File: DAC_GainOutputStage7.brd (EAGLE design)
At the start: 110 x 110.3 mm, 78 parts, among them J1 1935190, J3 SJ-63033A, U1 LM317MQDCYR, U2 LM317MQDCYR

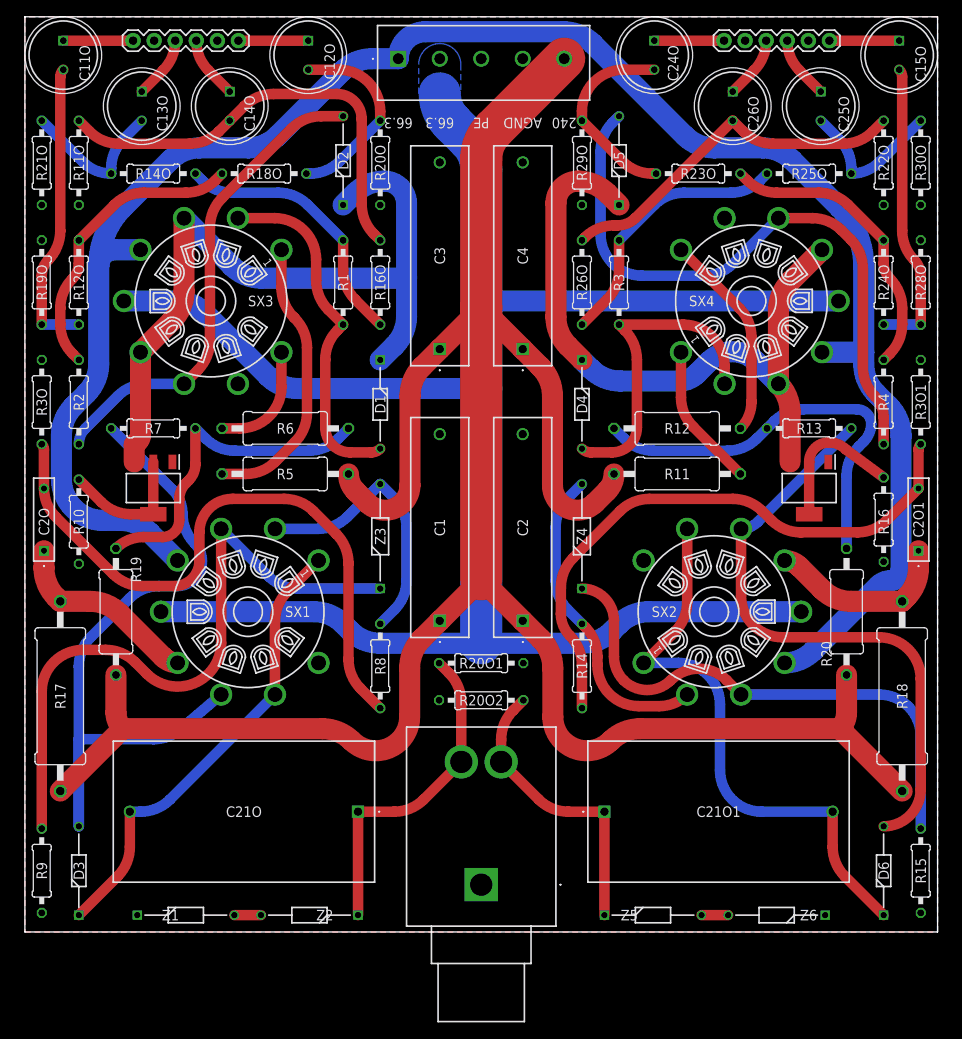
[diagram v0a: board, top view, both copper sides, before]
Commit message: Added new spice model and work on output stage
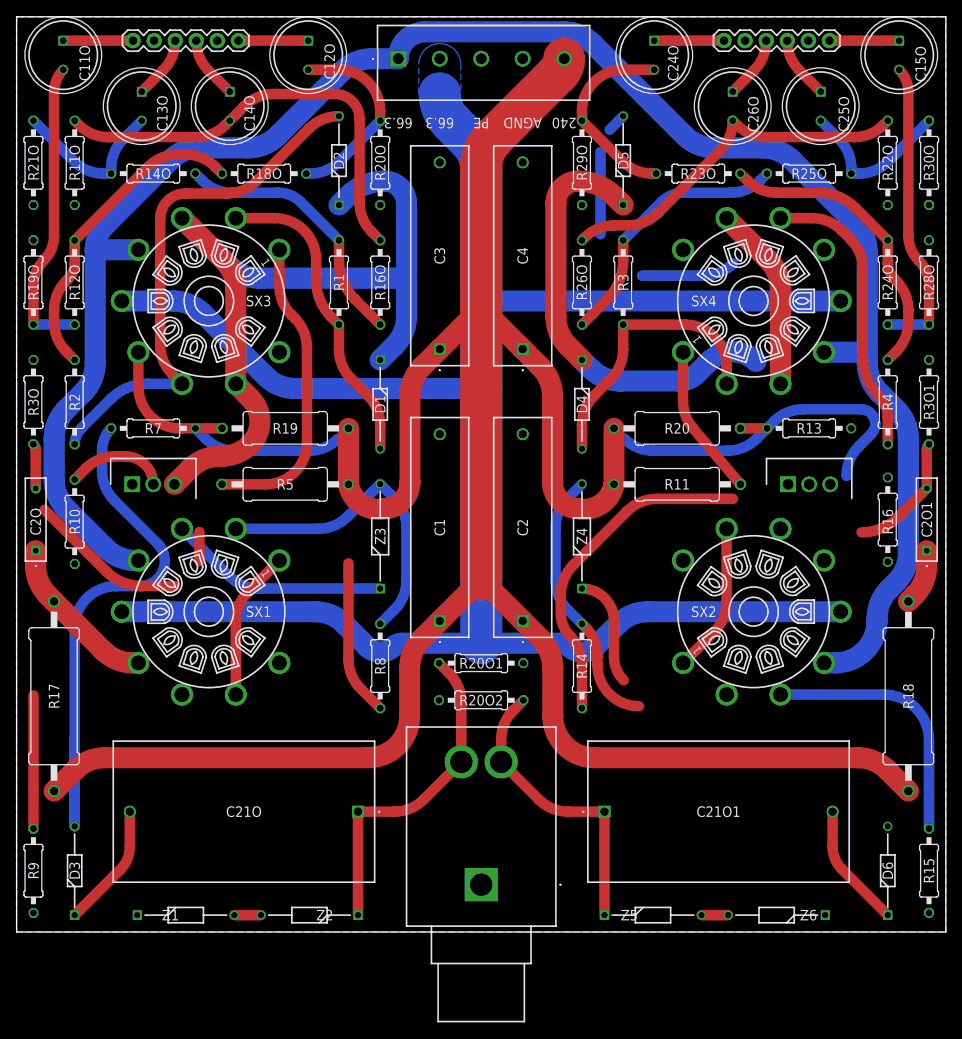
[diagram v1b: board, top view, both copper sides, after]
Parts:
- removed R12, R6: 3k, Dual Mono Amp Library:0411/15
- R11, R5: value 18k -> 15k
- U1, U2: value LM317MQDCYR -> LM317MTG; device Dual Mono Amp Library:SOT230P700X180-4N -> Dual Mono Amp Library:TO254P482X997X2018-3P
- moved R19 30.1 mm to (31.4, 55.7), turned to 0 degrees
- moved R20 30.1 mm to (78.6, 55.7), turned to 0 degrees
- moved SX2 4.76 mm to (87.8, 33.6)
- moved SX1 4.72 mm to (22.2, 33.6)
- moved U2 2.58 mm to (92.0, 49.0), turned to 0 degrees
- moved U1 2.58 mm to (12.9, 49.0), turned to 0 degrees
- moved R11 1.25 mm to (78.6, 49.0)
- moved R5 1.25 mm to (31.4, 49.0)
- moved R19O 1.00 mm to (1.03, 73.3)
- moved R21O 1.00 mm to (1.03, 87.7)
- moved R3O 1.00 mm to (1.03, 58.9)
- moved R9 1.00 mm to (1.03, 2.38)
- moved C2O1 1.00 mm to (108.7, 40.9)
- moved R15 1.00 mm to (109.0, 2.38)
- moved R28O 1.00 mm to (109.0, 73.3)
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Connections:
- removed net N$43: R6.1, SX3.9
- removed net N$44: R12.1, SX4.9
- net N$1: now also SX3.6; no longer R6.2
- net N$22: now also SX3.8; no longer SX3.6
- net N$37: no longer U1.4
- net N$38: no longer U2.4
- net N$7: now also SX4.8; no longer SX4.6
- net N$9: now also SX4.6; no longer R12.2
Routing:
- net N$29: track 71.6 -> 0.00 mm
- net N$26: track 77.5 -> 42.6 mm
- net N$3: track 67.6 -> 33.0 mm
- net N$16: track 76.4 -> 46.7 mm
- net N$44: track 25.0 -> 0.00 mm
- net N$18: track 55.7 -> 33.0 mm
- net N$23: track 88.1 -> 66.5 mm
- net N$27: track 62.6 -> 43.7 mm
- net N$5: track 75.8 -> 58.3 mm
- net N$38: track 17.5 -> 0.00 mm
- net N$17: track 71.5 -> 55.3 mm
- net N$40: track 22.3 -> 6.71 mm
- net N$43: track 13.4 -> 0.00 mm
- net 66.3VAC/2: track 236.7 -> 247.8 mm
- net N$22: track 90.5 -> 100.6 mm
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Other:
- board size 110 x 110.3 mm -> 112 x 110.3 mm

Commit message: Finished new output stage?
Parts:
- moved R16 0.25 mm to (104.0, 44.4)
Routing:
- net N$29: track 0.00 -> 66.2 mm
- net N$3: track 33.0 -> 66.0 mm
- net N$26: track 42.6 -> 71.5 mm
- net N$18: track 33.0 -> 57.0 mm
- net N$27: track 43.7 -> 62.3 mm
- net N$1: track 34.6 -> 16.3 mm
- net N$16: track 46.7 -> 64.7 mm
- net N$5: track 58.3 -> 76.1 mm
- net N$7: track 74.7 -> 92.4 mm
- net N$9: track 43.2 -> 27.3 mm
- net N$17: track 55.3 -> 69.2 mm
- net N$14: track 31.3 -> 43.6 mm
- net N$38: track 0.00 -> 11.7 mm
- net N$40: track 6.71 -> 18.3 mm
- net N$23: track 66.5 -> 68.9 mm
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
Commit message: Finished boards and spice models
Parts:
- R15, R9: value 698 -> 249
- R17, R18: value 1k -> 402
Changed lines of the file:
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@@
 <attribute name="NAME" x="42.825" y="27.052625" locked="yes" size="1.27" layer="25" rot="R270" align="center"/>
 </element>
-<element name="R9" library="Dual Mono Amp Library" library_urn="urn:adsk.eagle:library:47621477" package="0207/10" package3d_urn="urn:adsk.eagle:package:23491/2" value="698" x="1.030775" y="2.380775" locked="yes" smashed="yes" rot="R90">
-<attribute name="DESCRIPTION" value="Metal Film Resistors - Through Hole 698ohm 1% 0.6W Metal Film Resistor" x="1.030775" y="2.380775" locked="yes" size="1.778" layer="27" rot="R90" display="off"/>
+<element name="R9" library="Dual Mono Amp Library" library_urn="urn:adsk.eagle:library:47621477" package="0207/10" package3d_urn="urn:adsk.eagle:package:23491/2" value="249" x="1.030775" y="2.380775" locked="yes" smashed="yes" rot="R90">
+<attribute name="DESCRIPTION" value="Metal Film Resistors - Through Hole 249ohm 1% 0.6W Metal Film Resistor" x="1.030775" y="2.380775" locked="yes" size="1.778" layer="27" rot="R90" display="off"/>
 <attribute name="HEIGHT" value="mm" x="1.030775" y="2.380775" locked="yes" size="1.778" layer="27" rot="R90" display="off"/>
-<attribute name="MANUFACTURER_NAME" value="YAGEO" x="1.030775" y="2.380775" locked="yes" size="1.778" layer="27" rot="R90" display="off"/>
-<attribute name="MANUFACTURER_PART_NUMBER" value="MF0207FTE52-698R" x="1.030775" y="2.380775" locked="yes" size="1.778" layer="27" rot="R90" display="off"/>
+<attribute name="MANUFACTURER_NAME" value="VISHAY" x="1.030775" y="2.380775" locked="yes" size="1.778" layer="27" rot="R90" display="off"/>
+<attribute name="MANUFACTURER_PART_NUMBER" value="MBB02070C2490FRP00" x="1.030775" y="2.380775" locked="yes" size="1.778" layer="27" rot="R90" display="off"/>
 <attribute name="MOUSER_PART_NUMBER" value="" x="1.030775" y="2.380775" locked="yes" size="1.778" layer="27" rot="R90" display="off"/>
 <attribute name="MOUSER_PRICE-STOCK" value="" x="1.030775" y="2.380775" locked="yes" size="1.778" layer="27" rot="R90" display="off"/>
@@
 <attribute name="NAME" x="67.139346875" y="27.052625" locked="yes" size="1.27" layer="25" rot="R270" align="center"/>
 </element>
-<element name="R15" library="Dual Mono Amp Library" library_urn="urn:adsk.eagle:library:47621477" package="0207/10" package3d_urn="urn:adsk.eagle:package:23491/2" value="698" x="108.969225" y="2.380775" locked="yes" smashed="yes" rot="R90">
-<attribute name="DESCRIPTION" value="Metal Film Resistors - Through Hole 698ohm 1% 0.6W Metal Film Resistor" x="108.969225" y="2.380775" locked="yes" size="1.778" layer="27" rot="R90" display="off"/>
+<element name="R15" library="Dual Mono Amp Library" library_urn="urn:adsk.eagle:library:47621477" package="0207/10" package3d_urn="urn:adsk.eagle:package:23491/2" value="249" x="108.969225" y="2.380775" locked="yes" smashed="yes" rot="R90">
+<attribute name="DESCRIPTION" value="Metal Film Resistors - Through Hole 249ohm 1% 0.6W Metal Film Resistor" x="108.969225" y="2.380775" locked="yes" size="1.778" layer="27" rot="R90" display="off"/>
 <attribute name="HEIGHT" value="mm" x="108.969225" y="2.380775" locked="yes" size="1.778" layer="27" rot="R90" display="off"/>
-<attribute name="MANUFACTURER_NAME" value="YAGEO" x="108.969225" y="2.380775" locked="yes" size="1.778" layer="27" rot="R90" display="off"/>
-<attribute name="MANUFACTURER_PART_NUMBER" value="MF0207FTE52-698R" x="108.969225" y="2.380775" locked="yes" size="1.778" layer="27" rot="R90" display="off"/>
+<attribute name="MANUFACTURER_NAME" value="VISHAY" x="108.969225" y="2.380775" locked="yes" size="1.778" layer="27" rot="R90" display="off"/>
+<attribute name="MANUFACTURER_PART_NUMBER" value="MBB02070C2490FRP00" x="108.969225" y="2.380775" locked="yes" size="1.778" layer="27" rot="R90" display="off"/>
 <attribute name="MOUSER_PART_NUMBER" value="" x="108.969225" y="2.380775" locked="yes" size="1.778" layer="27" rot="R90" display="off"/>
 <attribute name="MOUSER_PRICE-STOCK" value="" x="108.969225" y="2.380775" locked="yes" size="1.778" layer="27" rot="R90" display="off"/>
@@
 <attribute name="NAME" x="67.139346875" y="42.68946875" locked="yes" size="1.27" layer="25" rot="R90" align="center"/>
 </element>
-<element name="R17" library="Dual Mono Amp Library" library_urn="urn:adsk.eagle:library:47621477" package="0617/22" package3d_urn="urn:adsk.eagle:package:23577/1" value="1k" x="3.515684375" y="23.415121875" locked="yes" smashed="yes" rot="R90">
-<attribute name="DESCRIPTION" value="Metal Film Resistors - Through Hole 1K OHM 2W 1%" x="3.515684375" y="23.415121875" locked="yes" size="1.778" layer="27" rot="R90" display="off"/>
+<element name="R17" library="Dual Mono Amp Library" library_urn="urn:adsk.eagle:library:47621477" package="0617/22" package3d_urn="urn:adsk.eagle:package:23577/1" value="402" x="3.515684375" y="23.415121875" locked="yes" smashed="yes" rot="R90">
+<attribute name="DESCRIPTION" value="Metal Film Resistors - Through Hole 402 OHM 2W 1%" x="3.515684375" y="23.415121875" locked="yes" size="1.778" layer="27" rot="R90" display="off"/>
 <attribute name="HEIGHT" value="mm" x="3.515684375" y="23.415121875" locked="yes" size="1.778" layer="27" rot="R90" display="off"/>
-<attribute name="MANUFACTURER_NAME" value="YAGEO" x="3.515684375" y="23.415121875" locked="yes" size="1.778" layer="27" rot="R90" display="off"/>
-<attribute name="MANUFACTURER_PART_NUMBER" value="MFR200FRF52-1K" x="3.515684375" y="23.415121875" locked="yes" size="1.778" layer="27" rot="R90" display="off"/>
+<attribute name="MANUFACTURER_NAME" value="VISHAY" x="3.515684375" y="23.415121875" locked="yes" size="1.778" layer="27" rot="R90" display="off"/>
+<attribute name="MANUFACTURER_PART_NUMBER" value="RWR80S4020FRB12" x="3.515684375" y="23.415121875" locked="yes" size="1.778" layer="27" rot="R90" display="off"/>
 <attribute name="MOUSER_PART_NUMBER" value="" x="3.515684375" y="23.415121875" locked="yes" size="1.778" layer="27" rot="R90" display="off"/>
 <attribute name="MOUSER_PRICE-STOCK" value="" x="3.515684375" y="23.415121875" locked="yes" size="1.778" layer="27" rot="R90" display="off"/>
 <attribute name="NAME" x="3.515684375" y="23.415121875" locked="yes" size="1.27" layer="25" rot="R90" align="center"/>
 </element>
-<element name="R18" library="Dual Mono Amp Library" library_urn="urn:adsk.eagle:library:47621477" package="0617/22" package3d_urn="urn:adsk.eagle:package:23577/1" value="1k" x="106.484315625" y="23.415121875" locked="yes" smashed="yes" rot="R270">
-<attribute name="DESCRIPTION" value="Metal Film Resistors - Through Hole 1K OHM 2W 1%" x="106.484315625" y="23.415121875" locked="yes" size="1.778" layer="27" rot="R270" display="off"/>
+<element name="R18" library="Dual Mono Amp Library" library_urn="urn:adsk.eagle:library:47621477" package="0617/22" package3d_urn="urn:adsk.eagle:package:23577/1" value="402" x="106.484315625" y="23.415121875" locked="yes" smashed="yes" rot="R270">
+<attribute name="DESCRIPTION" value="Metal Film Resistors - Through Hole 402 OHM 2W 1%" x="106.484315625" y="23.415121875" locked="yes" size="1.778" layer="27" rot="R270" display="off"/>
 <attribute name="HEIGHT" value="mm" x="106.484315625" y="23.415121875" locked="yes" size="1.778" layer="27" rot="R270" display="off"/>
-<attribute name="MANUFACTURER_NAME" value="YAGEO" x="106.484315625" y="23.415121875" locked="yes" size="1.778" layer="27" rot="R270" display="off"/>
-<attribute name="MANUFACTURER_PART_NUMBER" value="MFR200FRF52-1K" x="106.484315625" y="23.415121875" locked="yes" size="1.778" layer="27" rot="R270" display="off"/>
+<attribute name="MANUFACTURER_NAME" value="VISHAY" x="106.484315625" y="23.415121875" locked="yes" size="1.778" layer="27" rot="R270" display="off"/>
+<attribute name="MANUFACTURER_PART_NUMBER" value="RWR80S4020FRB12" x="106.484315625" y="23.415121875" locked="yes" size="1.778" layer="27" rot="R270" display="off"/>
 <attribute name="MOUSER_PART_NUMBER" value="" x="106.484315625" y="23.415121875" locked="yes" size="1.778" layer="27" rot="R270" display="off"/>
 <attribute name="MOUSER_PRICE-STOCK" value="" x="106.484315625" y="23.415121875" locked="yes" size="1.778" layer="27" rot="R270" display="off"/>
@@
 <mfgpreviewcolor name="substratecolor" color="0xFF786E46"/>
 </mfgpreviewcolors>
+<errors>
+</errors>
 </board>
 </drawing>
